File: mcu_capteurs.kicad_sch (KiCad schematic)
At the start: 72 parts, among them J4 STLINK, SW1 435431019840, SW2 SW_Push, U2 TCA9517DR, U3 WSEN-PDUS, U4 STM32G474CEUx, Y1 16 MHz

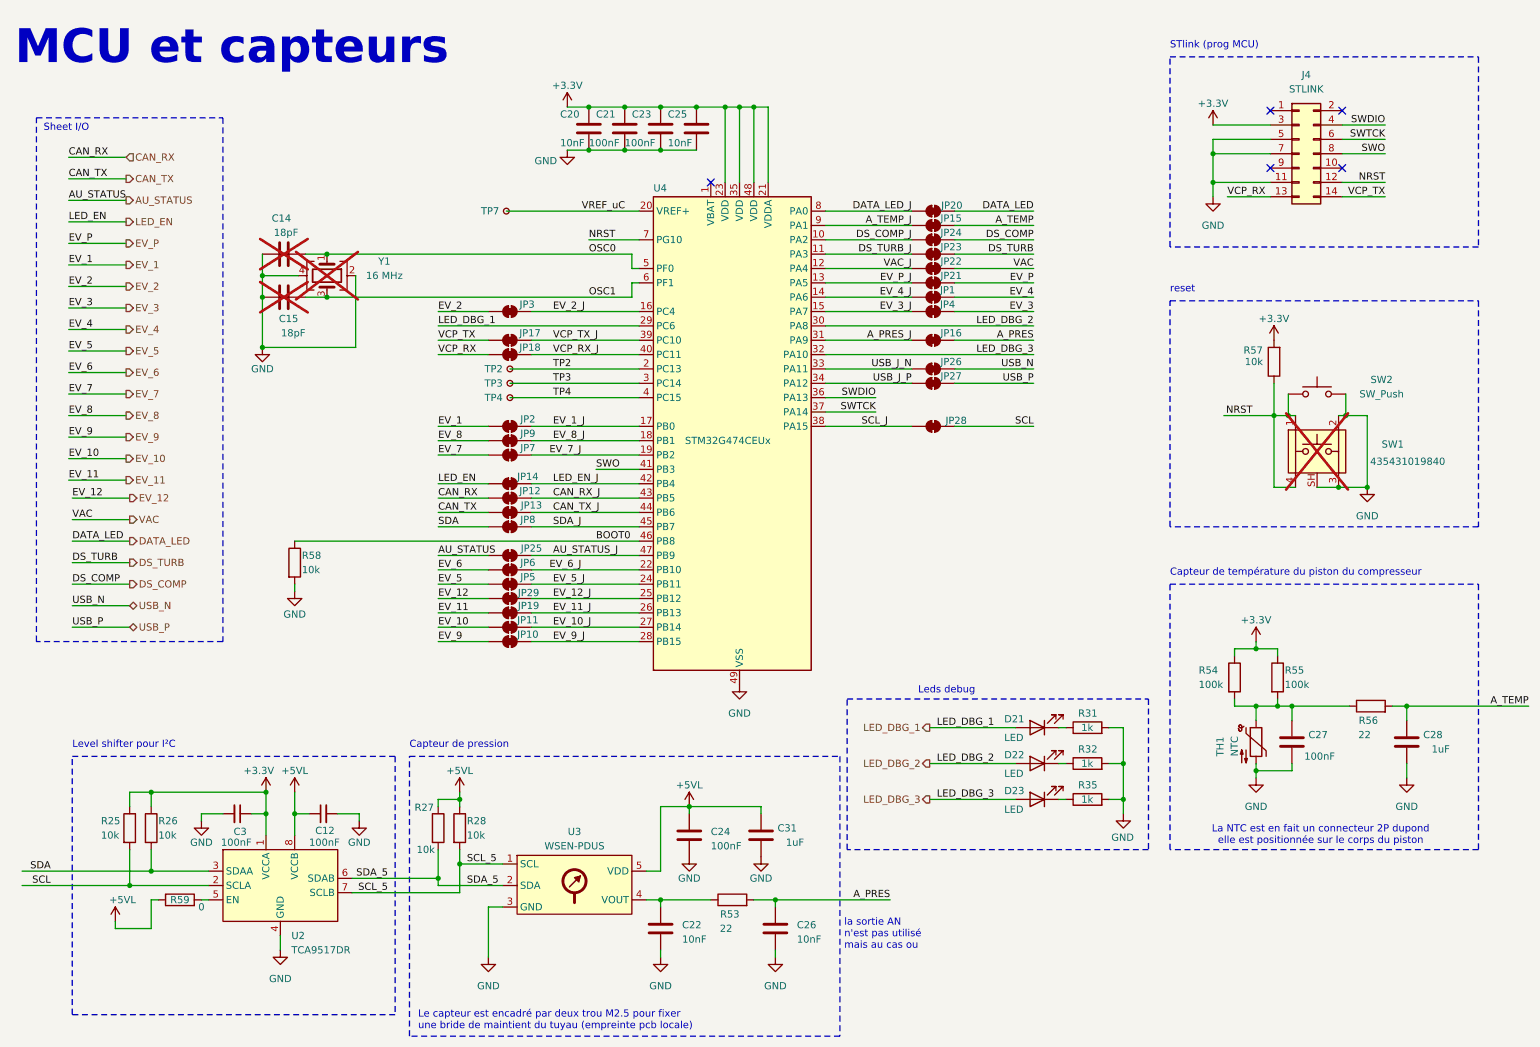
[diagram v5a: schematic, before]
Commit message: mise à jour du schema après la coupe de belgique
- modification du circuit d'AU (SW_AU 24V->3.3V)
- modification du pinout de J3: ajout du CAN (suppression de J8) et du RST_EXT
- ajout d'un circuit de reset externe (configurable via 3-jumper)
- ajout d'un connecteur dédié pour un bouton reset externe
- ajout d'un debounce sur le switch reset
- mise à jour du routage et serigraphie
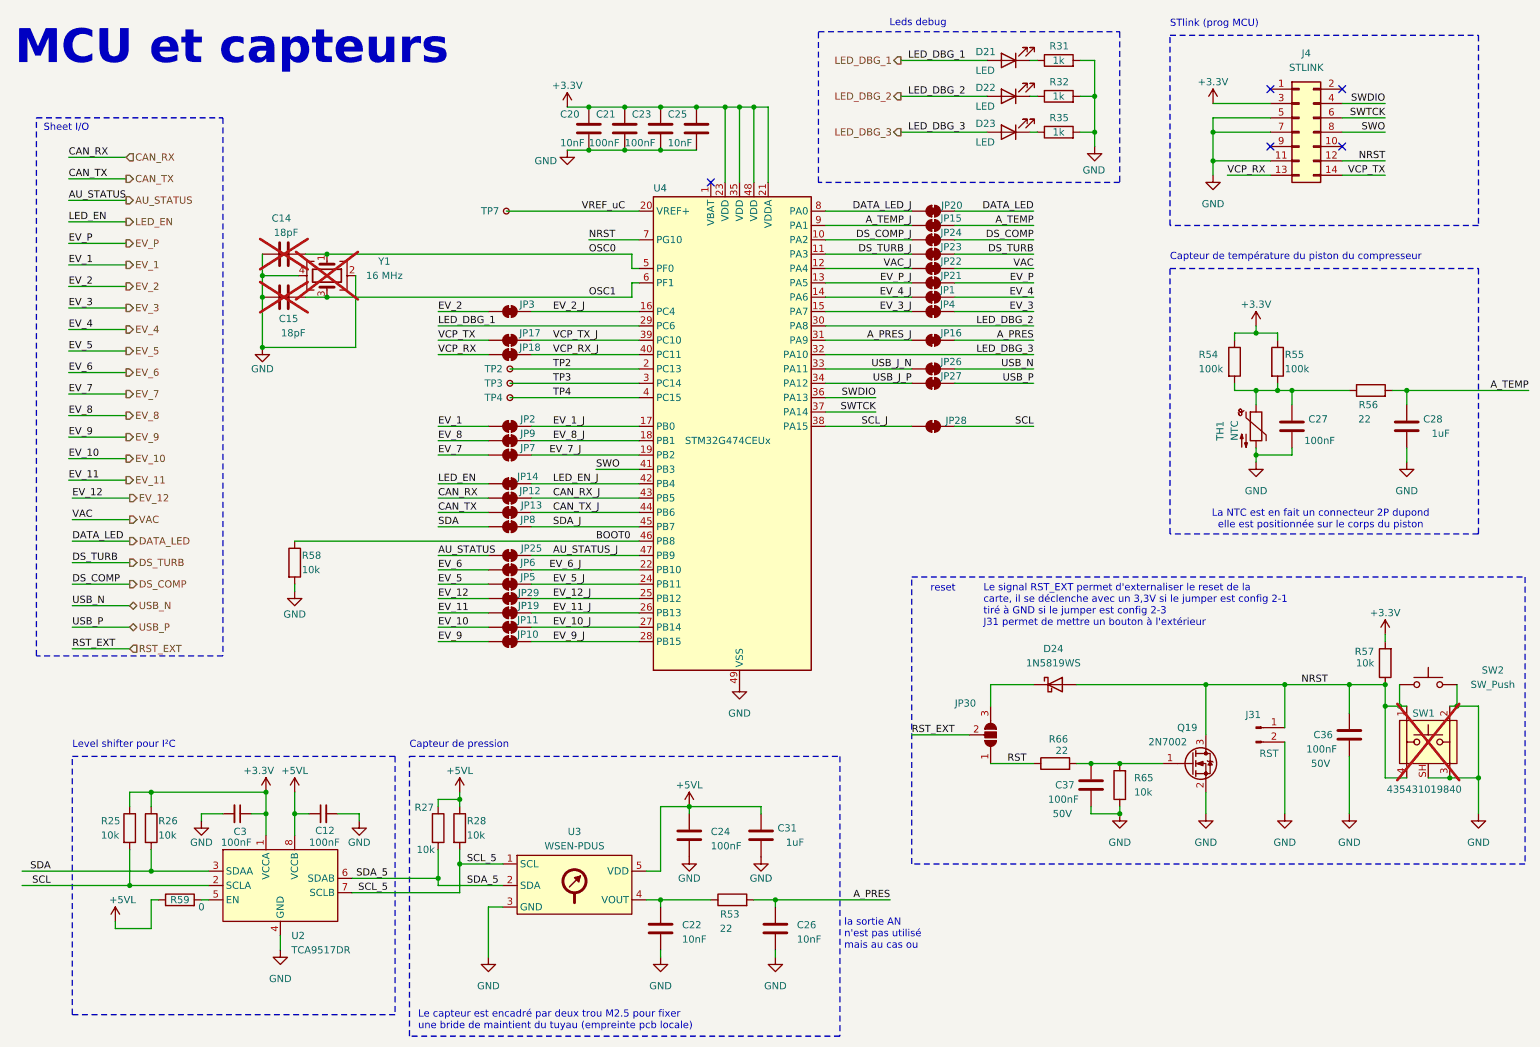
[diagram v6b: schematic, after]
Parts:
- added C36, C37: 100nF, Capacitor_SMD:C_0603_1608Metric, symbol Device:C
- added D24: 1N5819WS, Diode_SMD:D_SOD-323_HandSoldering, symbol Device:D_Schottky
- added J31: RST, Connector_PinHeader_2.54mm:PinHeader_1x02_P2.54mm_Vertical, symbol Connector:Conn_01x02_Pin
- added JP30: SolderJumper_3_Open, Jumper:SolderJumper-3_P1.3mm_Open_RoundedPad1.0x1.5mm, symbol Jumper:SolderJumper_3_Open
- added Q19: 2N7002, Package_TO_SOT_SMD:SOT-23, symbol Transistor_FET:2N7002
- added R65: 10k, Resistor_SMD:R_0603_1608Metric, symbol Device:R
- added R66: 22, Resistor_SMD:R_0603_1608Metric, symbol Device:R
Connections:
- net GND: now also C36.2, C37.2, J31.2 (Pin_2), Q19.2 (S), R65.1
- net NRST: now also C36.1, D24.2 (A), J31.1 (Pin_1), Q19.3 (D)
- new net: C37.1, Q19.1 (G), R65.2, R66.2
- new net: D24.1 (K), JP30.3 (B)
- new net RST: JP30.1 (A), R66.1
- new net RST_EXT: JP30.2 (C)
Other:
- note added: "Le signal RST_EXT permet d'externaliser le reset de la carte, il se déclenche avec un 3,3V si le jumper est config 2-1 tiré à GND si le jumper est config 2-3 J31 permet de mettre un bouton à l'extérieur"
- moved on the sheet: C27, C28, D21, D22, D23, J4, R31, R32, R35, R54, R55, R56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

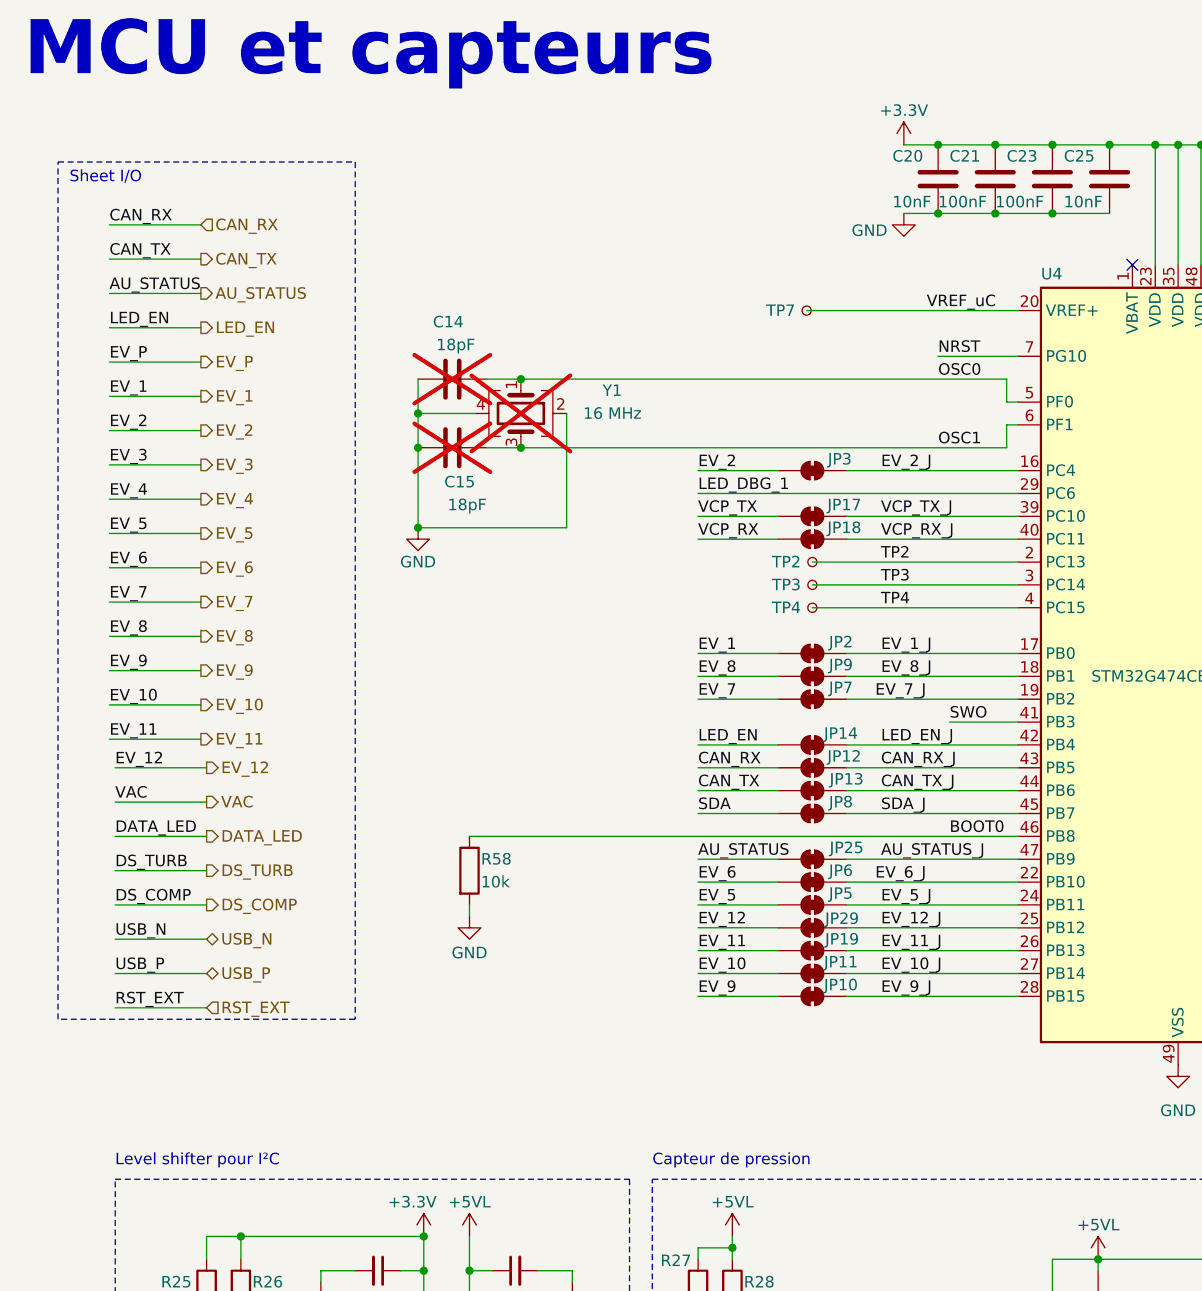
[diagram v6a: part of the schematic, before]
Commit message: Maj crystal et connection therminque DC-DC
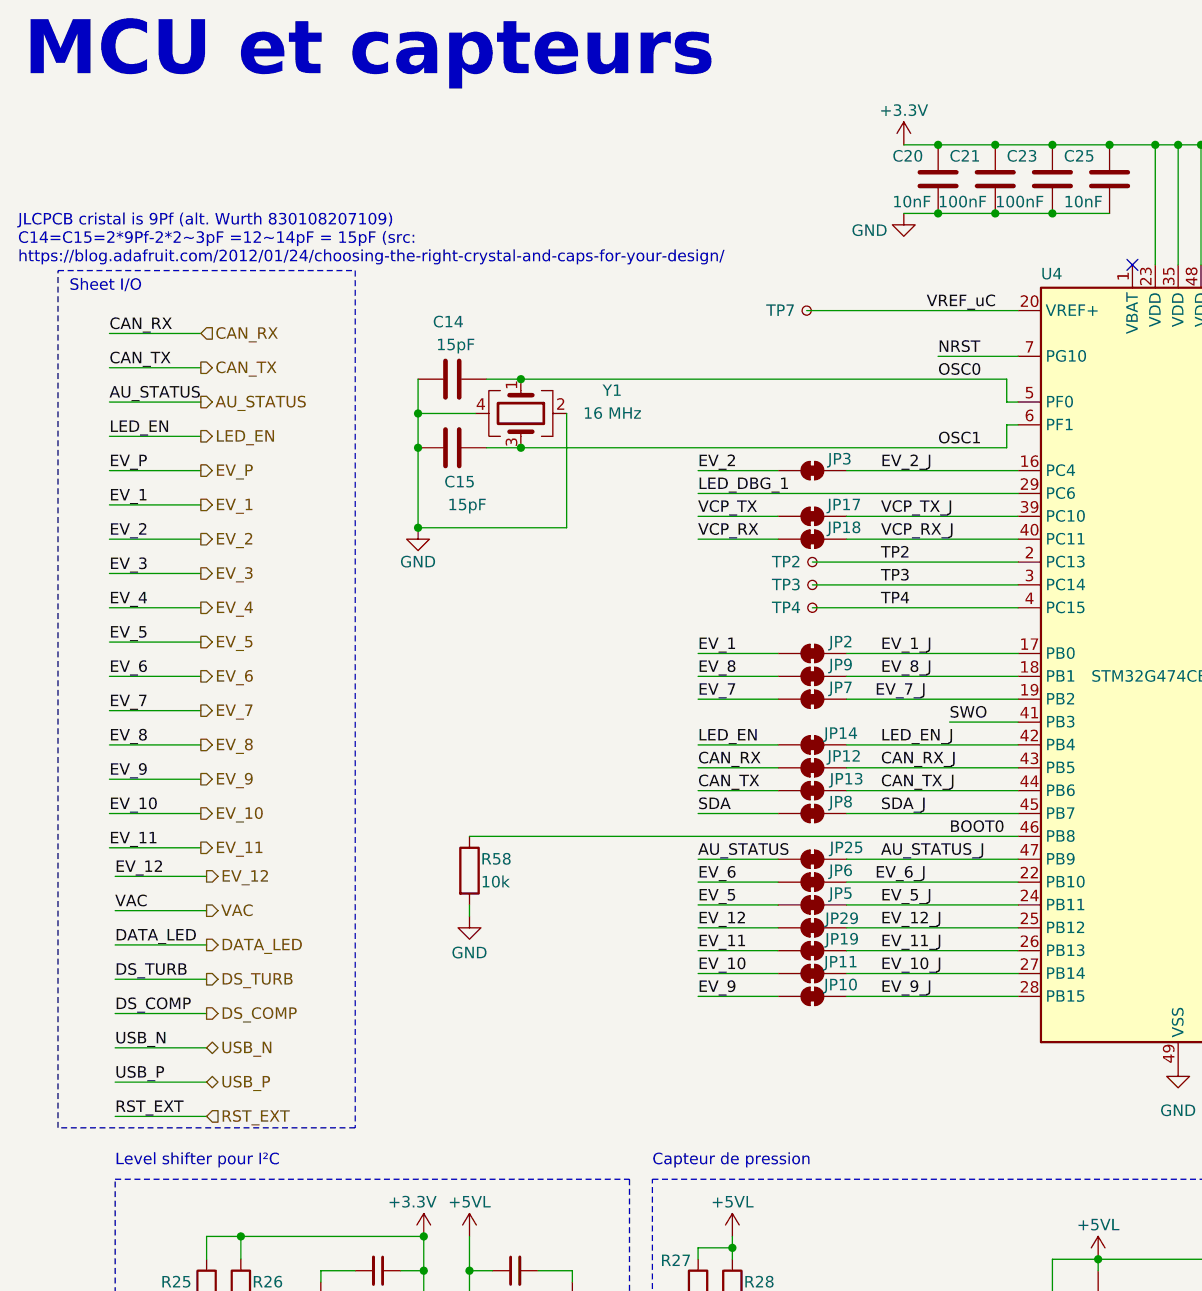
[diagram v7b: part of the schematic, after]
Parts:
- C14, C15: value 18pF -> 15pF; now fitted; now in the parts list
- Y1: LCSC (none) -> C13738; now fitted; now in the parts list
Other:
- note added: "JLCPCB cristal is 9Pf (alt. Wurth 830108207109) C14=C15=2*9Pf-2*2~3pF =12~14pF = 15pF (src: https://blog.adafruit.com/2012/01/24/choosing-the-right-crystal-and-caps-for-your-design/"
